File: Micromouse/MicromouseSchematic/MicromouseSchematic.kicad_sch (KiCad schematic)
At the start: 2 parts, among them U5 STM32F746VETx

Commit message: tof version 1
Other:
- sheet ToF ports: added INT (ToF); removed Vin (2.8 V)
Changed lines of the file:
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@@
+	(wire
+		(pts
+			(xy 200.66 85.09) (xy 205.74 85.09)
+		)
+		(stroke
+			(width 0)
+			(type default)
+		)
+	)
 	(wire
 		(pts
@@
 	)
 	(symbol
+		(lib_id "power:+3V3")
+		(at 205.74 85.09 0)
+		(unit 1)
+		(exclude_from_sim no)
+		(in_bom yes)
+		(on_board yes)
+		(dnp no)
+		(fields_autoplaced yes)
+		(property "Reference" "#PWR047"
+			(at 205.74 88.9 0)
+			(effects
+				(font
+					(size 1.27 1.27)
+				)
+				(hide yes)
+			)
+		)
+		(property "Value" "3V3"
+			(at 205.74 80.01 0)
+			(effects
+				(font
+					(size 1.27 1.27)
+				)
+			)
+		)
+		(property "Footprint" ""
+			(at 205.74 85.09 0)
+			(effects
+				(font
+					(size 1.27 1.27)
+				)
+				(hide yes)
+			)
+		)
+		(property "Datasheet" ""
+			(at 205.74 85.09 0)
+			(effects
+				(font
+					(size 1.27 1.27)
+				)
+				(hide yes)
+			)
+		)
+		(property "Description" "Power symbol creates a global label with name \"+3V3\""
+			(at 205.74 85.09 0)
+			(effects
+				(font
+					(size 1.27 1.27)
+				)
+				(hide yes)
+			)
+		)
+		(pin "1"
+		)
+		(instances
+			(project ""
+				(path "/0dcfab91-6b00-43c0-ac0b-8c301cb559e5"
+					(reference "#PWR047")
+					(unit 1)
+				)
+			)
+		)
+	)
+	(symbol
 		(lib_id "SFH 3015 FA:SFH_3015_FA")
 		(at 123.19 107.95 0)
@@
 			)
 		)
-		(pin "Vin (2.8 V)" input
-			(at 218.44 114.3 180)
-			(effects
-				(font
+		(pin "INT (ToF)" input
+			(at 218.44 129.54 180)
+			(effects
+				(font

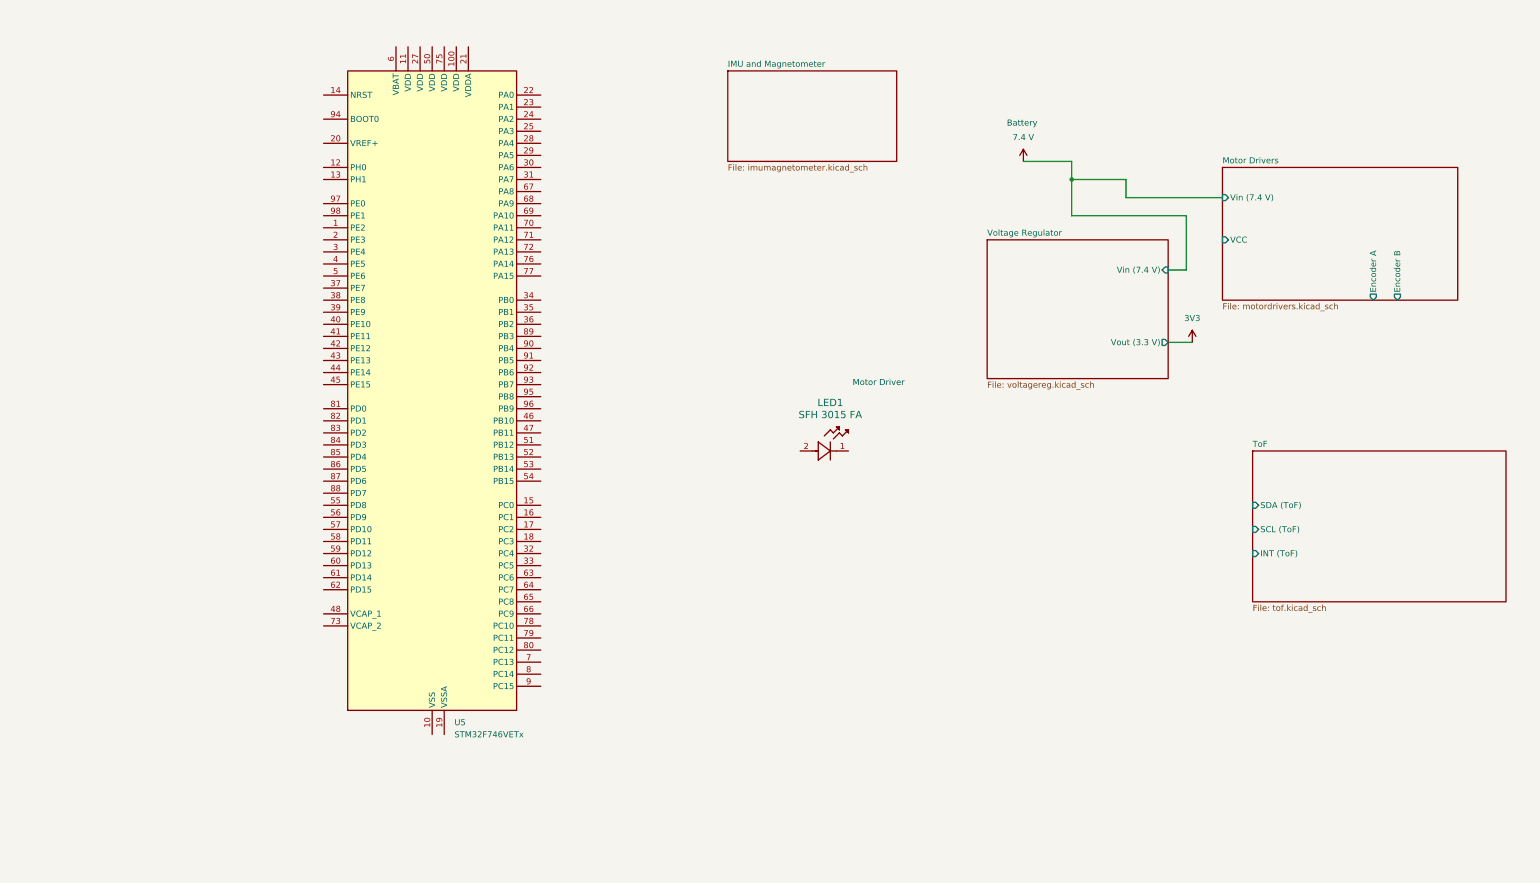
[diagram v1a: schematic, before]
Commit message: Added microcontroller schematics
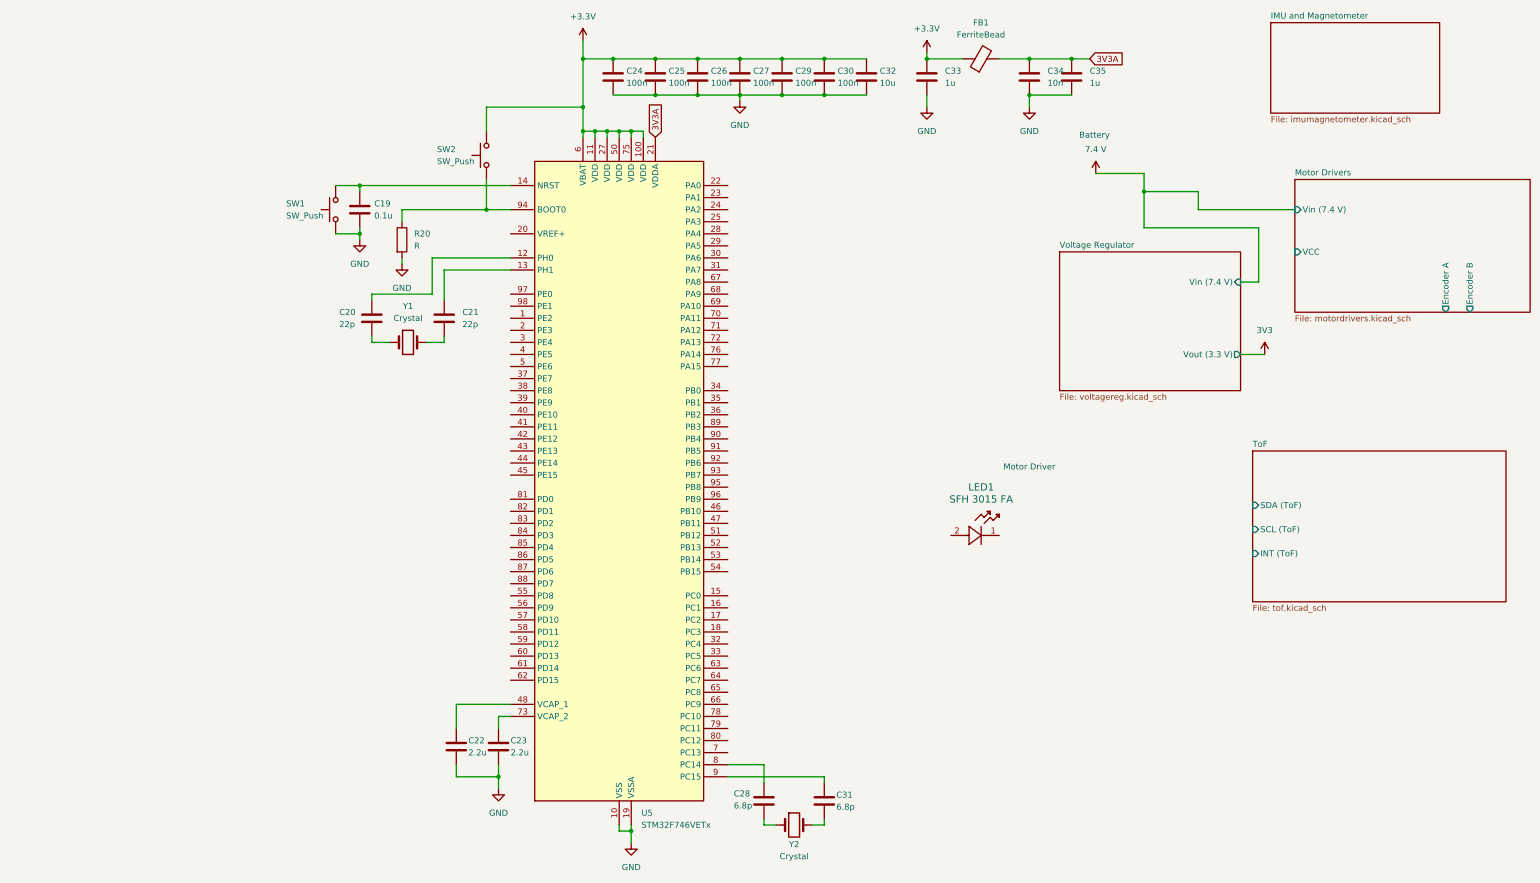
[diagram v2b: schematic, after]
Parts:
- added C19: 0.1u, symbol Device:C
- added C20, C21: 22p, symbol Device:C
- added C22, C23: 2.2u, symbol Device:C
- added C24, C25, C26, C27, C29, C30: 100n, symbol Device:C
- added C28, C31: 6.8p, symbol Device:C
- added C32: 10u, symbol Device:C
- added C33, C35: 1u, symbol Device:C
- added C34: 10n, symbol Device:C
- added FB1: FerriteBead, symbol Device:FerriteBead
- added R20: R, symbol Device:R
- added SW1, SW2: SW_Push, symbol Switch:SW_Push
- added Y1, Y2: Crystal, symbol Device:Crystal
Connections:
- net GND: now reaches U5.10 (VSS), U5.26 (VSS), U5.49 (VSS), U5.74 (VSS), U5.99 (VSS)
- net GND: now also U5.19 (VSSA), C19.2, C22.2, C23.2, C24.2, C25.2, C26.2, C27.2, C29.2, C30.2, C32.2, C33.2, C34.2, C35.2, R20.2, SW1.1
- net +3.3V: now reaches U5.100 (VDD)
- net +3.3V: now also U5.11 (VDD), U5.27 (VDD), U5.50 (VDD), U5.6 (VBAT), U5.75 (VDD), C24.1, C25.1, C26.1, C27.1, C29.1, C30.1, C32.1, C33.1, FB1.1, SW2.2
- net at U5.12 (PH0): now also C20.1
- net at U5.13 (PH1): now also C21.1
- net at U5.14 (NRST): now also C19.1, SW1.2
- net 3V3A: now reaches U5.21 (VDDA)
- net 3V3A: now also C34.1, C35.1, FB1.2
- net at U5.48 (VCAP_1): now also C22.1
- net at U5.73 (VCAP_2): now also C23.1
- net at U5.8 (PC14): now also C28.1
- net at U5.9 (PC15): now also C31.1
- net at U5.94 (BOOT0): now also R20.1, SW2.1
- new net: C20.2, Y1.1
- new net: C21.2, Y1.2
- new net: C28.2, Y2.1
- new net: C31.2, Y2.2
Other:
- moved on the sheet: LED1

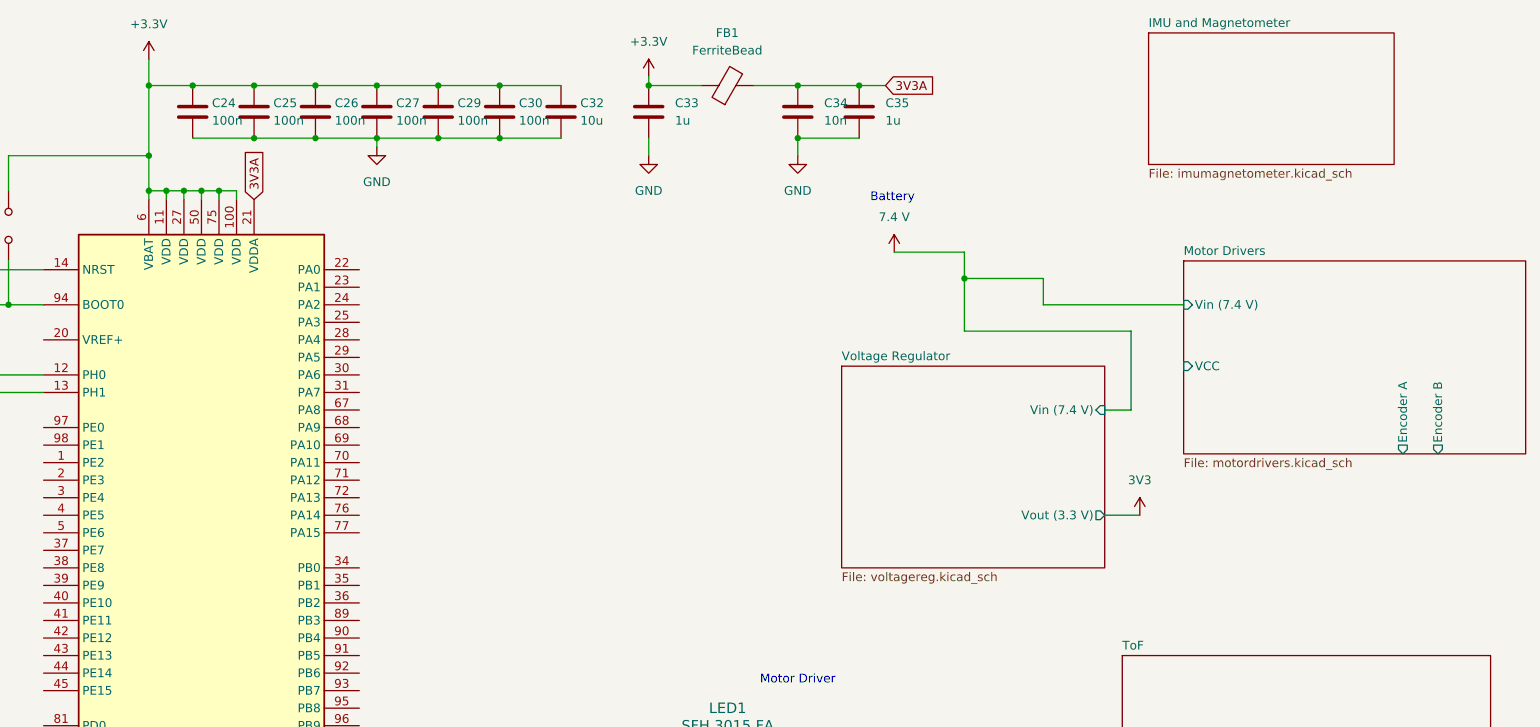
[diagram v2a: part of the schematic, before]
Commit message: changed motor driver schematics
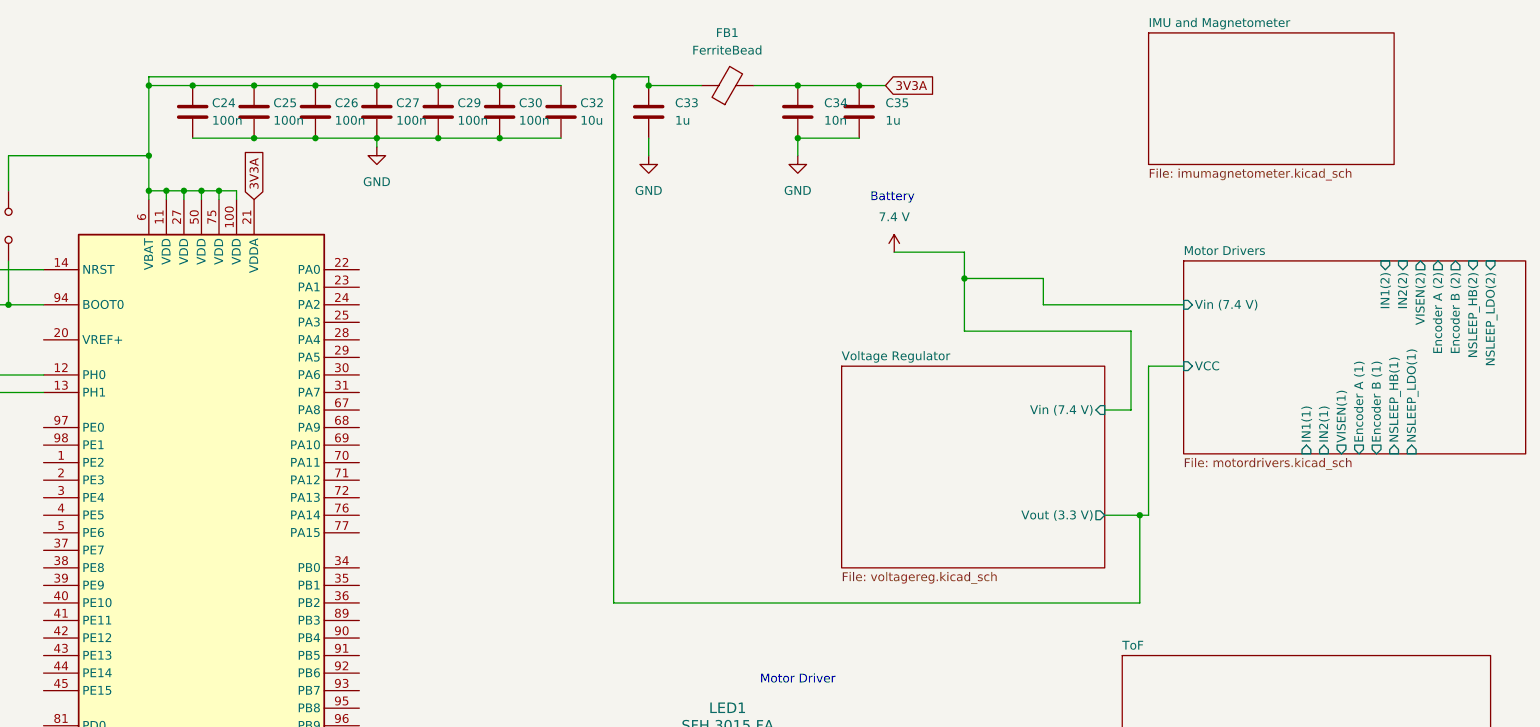
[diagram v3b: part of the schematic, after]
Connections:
- net +3.3V is gone; now on net Motor Drivers/VCC: C24.1, C25.1, C26.1, C27.1, C29.1, C30.1, C32.1, C33.1, FB1.1, SW2.2, U5.100 (VDD), U5.11 (VDD), U5.27 (VDD), U5.50 (VDD), U5.6 (VBAT), U5.75 (VDD)
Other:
- sheet Motor Drivers ports: added Encoder A (1), Encoder A (2), Encoder B (1), Encoder B (2), IN1(1), IN1(2), IN2(1), IN2(2), NSLEEP_HB(1), NSLEEP_HB(2), NSLEEP_LDO(1), NSLEEP_LDO(2), VISEN(1), VISEN(2); removed Encoder A, Encoder B

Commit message: Made changesto IMU/magnetometer
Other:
- sheet IMU and Magnetometer ports: added 3.3V, INT(Magnetometer), INT1 (IMU), INT2 (IMU), SCL (IMU), SCL(Magnetometer), SDA (IMU), SDA(Magnetometer); removed none
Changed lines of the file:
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@@
+			)
+		)
+		(pin "INT1 (IMU)" output
+			(at 222.25 19.05 180)
+			(effects
+				(font
+					(size 1.27 1.27)
+				)
+				(justify left)
+			)
+		)
+		(pin "SDA (IMU)" input
+			(at 222.25 21.59 180)
+			(effects
+				(font
+					(size 1.27 1.27)
+				)
+				(justify left)
+			)
+		)
+		(pin "INT2 (IMU)" bidirectional
+			(at 222.25 20.32 180)
+			(effects
+				(font
+					(size 1.27 1.27)
+				)
+				(justify left)
+			)
+		)
+		(pin "SDA(Magnetometer)" input
+			(at 222.25 31.75 180)
+			(effects
+				(font
+					(size 1.27 1.27)
+				)
+				(justify left)
+			)
+		)
+		(pin "SCL(Magnetometer)" input
+			(at 222.25 34.29 180)
+			(effects
+				(font
+					(size 1.27 1.27)
+				)
+				(justify left)
+			)
+		)
+		(pin "INT(Magnetometer)" output
+			(at 222.25 29.21 180)
+			(effects
+				(font
+					(size 1.27 1.27)
+				)
+				(justify left)
+			)
+		)
+		(pin "SCL (IMU)" input
+			(at 222.25 22.86 180)
+			(effects
+				(font
+					(size 1.27 1.27)
+				)
+				(justify left)
+			)
+		)
+		(pin "3.3V" input
+			(at 255.27 36.83 270)
+			(effects
+				(font
+					(size 1.27 1.27)
+				)
+				(justify left)
 			)
 		)

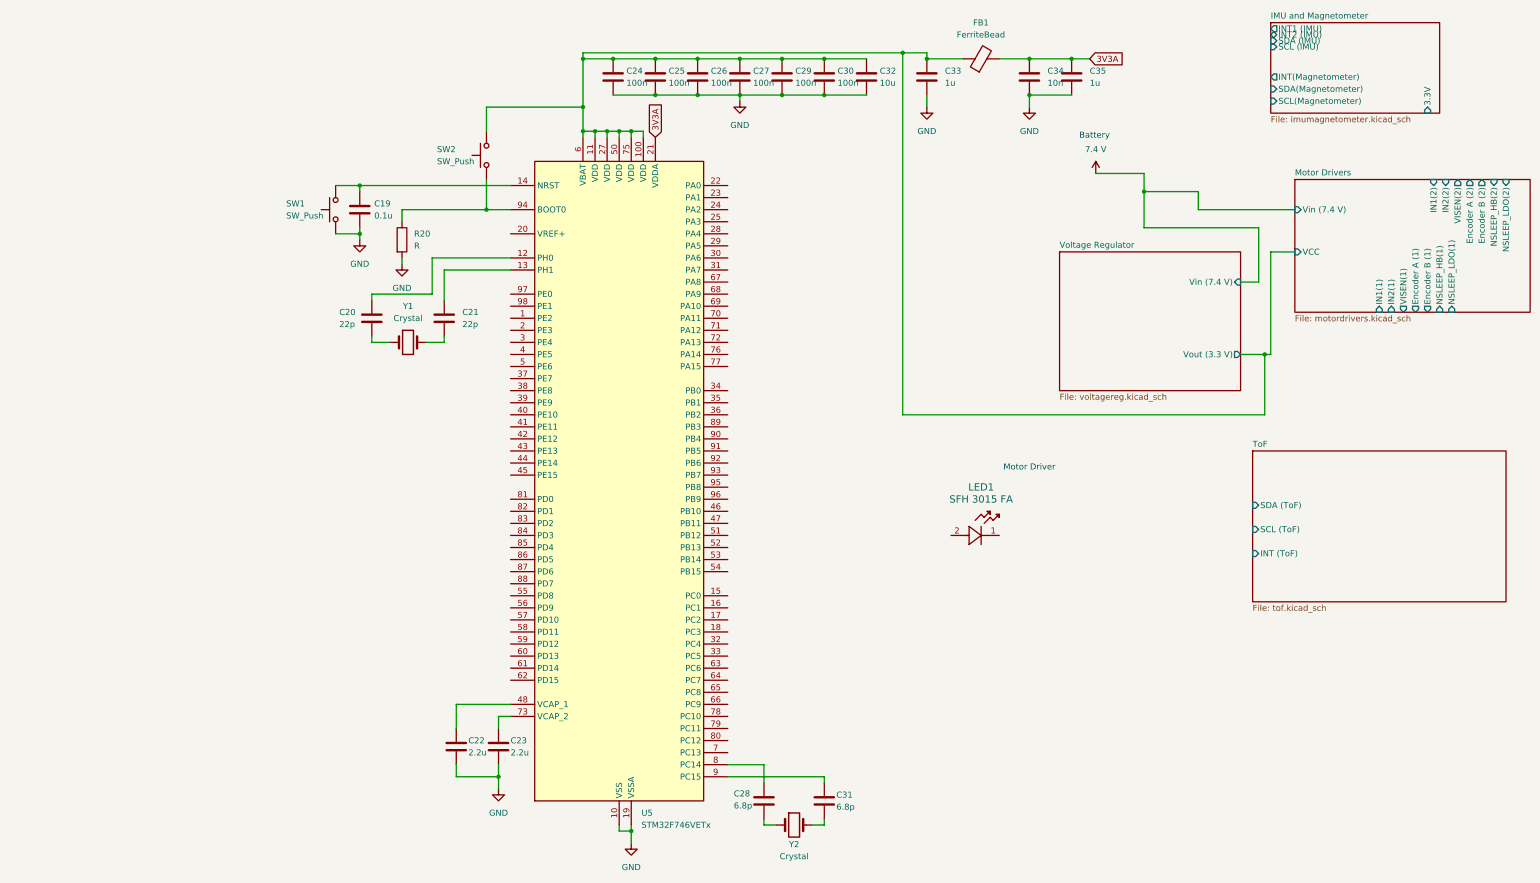
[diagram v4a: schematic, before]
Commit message: Added IR, programming header, i2c & timer pins
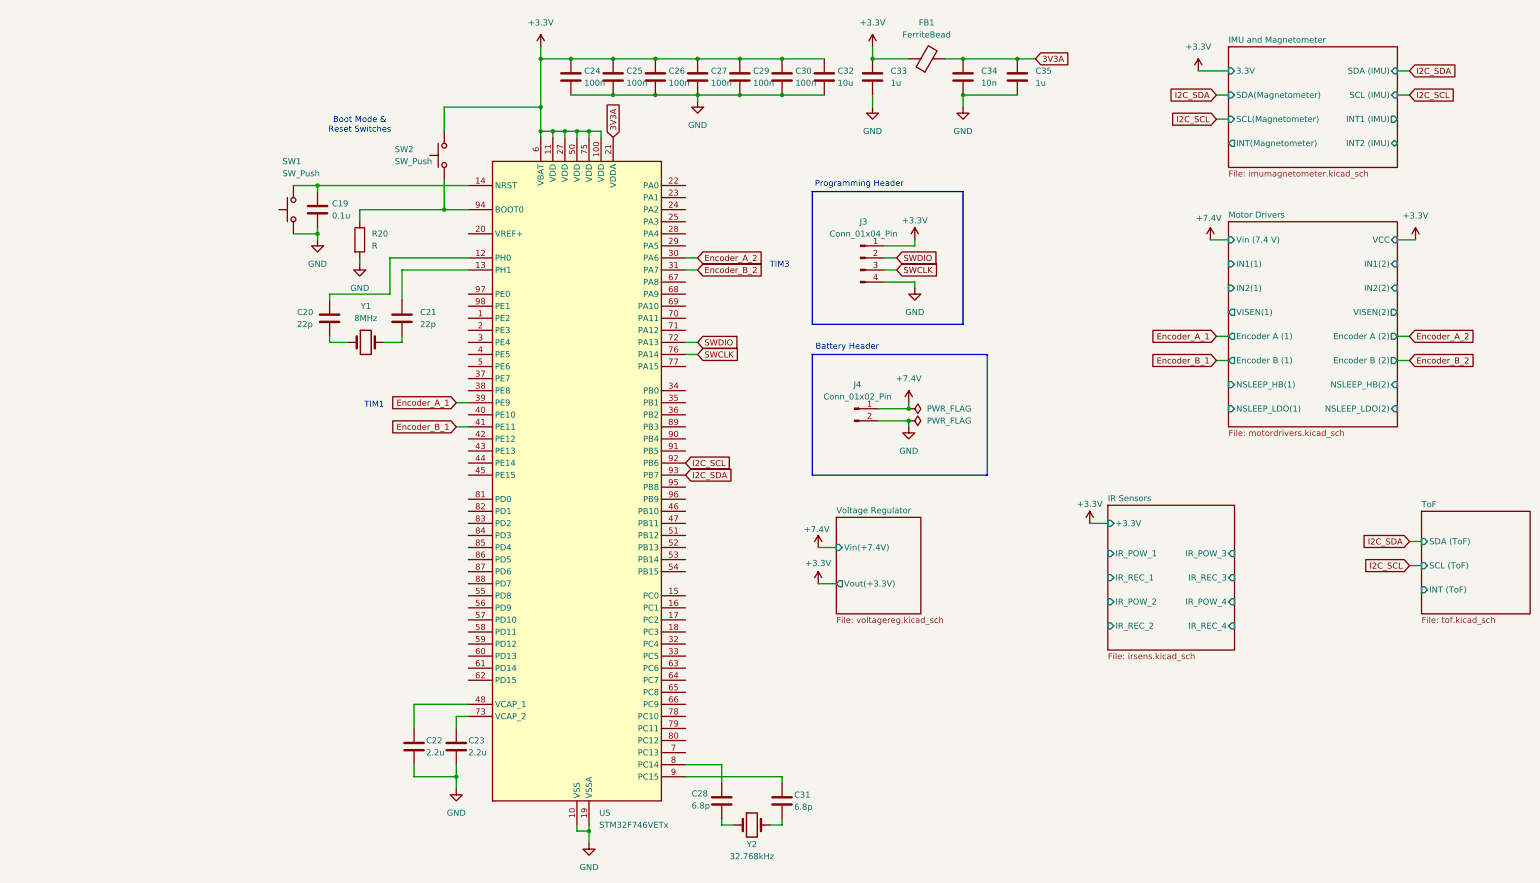
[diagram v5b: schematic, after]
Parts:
- removed LED1: SFH 3015 FA, LED_SFH 3015 FA_OSR, symbol SFH 3015 FA:SFH_3015_FA
- added J3: Conn_01x04_Pin, symbol Connector:Conn_01x04_Pin
- added J4: Conn_01x02_Pin, symbol Connector:Conn_01x02_Pin
- Y1: value Crystal -> 8MHz
- Y2: value Crystal -> 32.768kHz
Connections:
- net GND: now also J3.4 (Pin_4), J4.2 (Pin_2)
- net Encoder_A_2: now reaches U5.30 (PA6)
- net Encoder_B_2: now reaches U5.31 (PA7)
- net Encoder_A_1: now reaches U5.39 (PE9)
- net Encoder_B_1: now reaches U5.41 (PE11)
- net SWDIO: now reaches U5.72 (PA13)
- net SWDIO: now also J3.2 (Pin_2)
- net SWCLK: now reaches U5.76 (PA14)
- net SWCLK: now also J3.3 (Pin_3)
- net I2C_SCL: now reaches U5.92 (PB6)
- net I2C_SDA: now reaches U5.93 (PB7)
- net Motor Drivers/VCC renamed +3.3V
- net +3.3V: now also J3.1 (Pin_1)
- new net +7.4V: J4.1 (Pin_1)
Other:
- added sheet IR Sensors (irsens.kicad_sch)
- sheet Voltage Regulator ports: added Vin(+7.4V), Vout(+3.3V); removed Vin (7.4 V), Vout (3.3 V)
- note added: "Battery Header"
- note added: "Boot Mode & Reset Switches"
- note added: "Programming Header"
- note added: "TIM1"
- note added: "TIM3"
- note removed: "Battery"
- note removed: "Motor Driver"
- moved on the sheet: C19, C20, C21, C22, C23, C24, C25, C26, C27, C28, C29, C30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

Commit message: added some stuff
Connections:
- net I2C_SCL: no longer names the net of U5.92 (PB6)
- net I2C_SDA: no longer names the net of U5.93 (PB7)
- no-connect marks 0 -> 73
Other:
- sheet ToF ports: added +3.3V; removed none
